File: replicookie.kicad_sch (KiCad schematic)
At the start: 0 parts

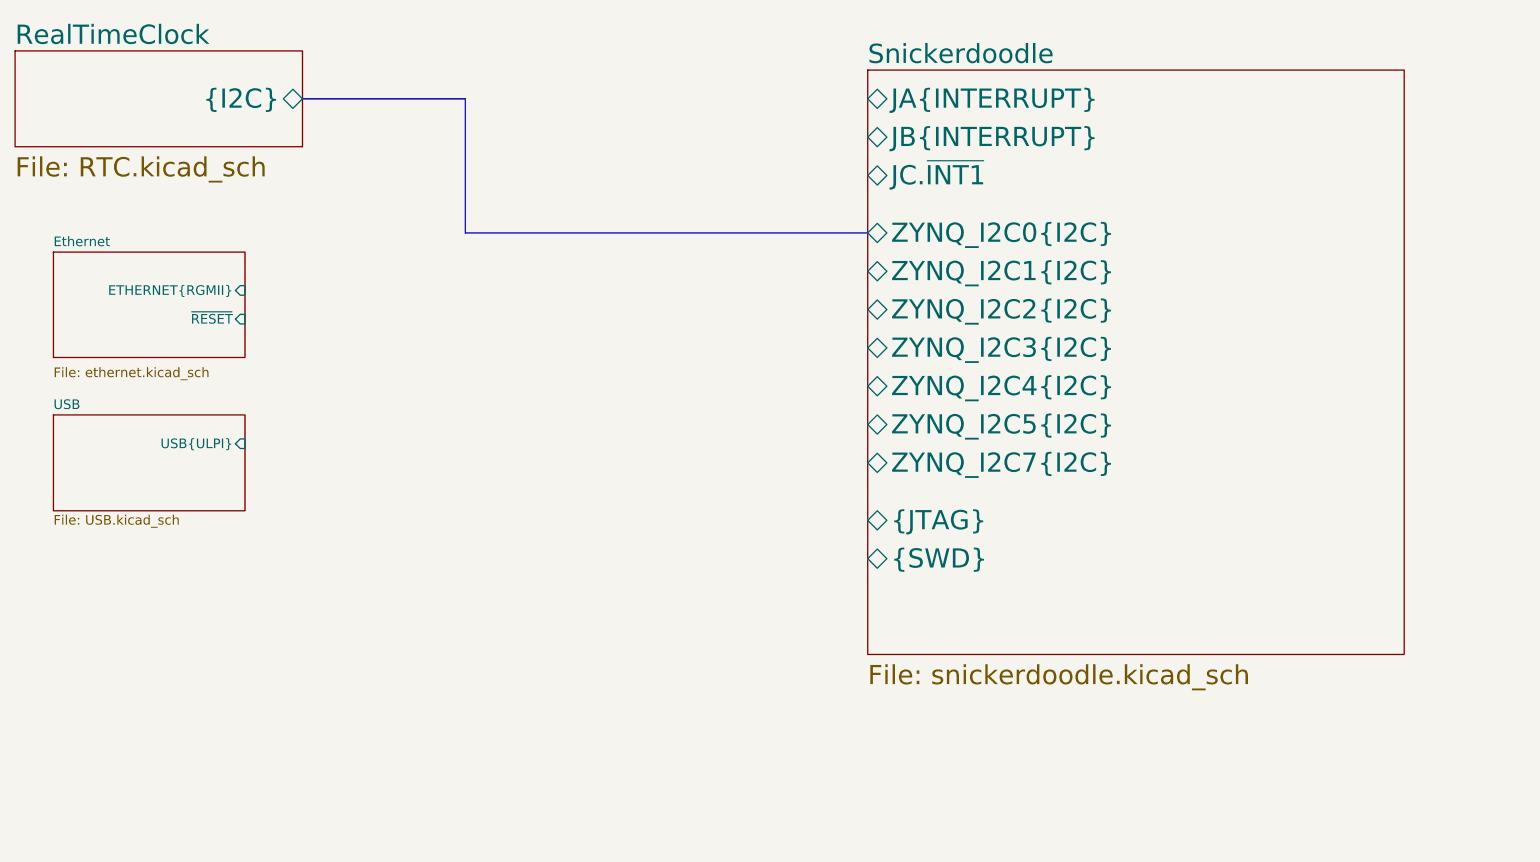
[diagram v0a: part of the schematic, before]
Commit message: Connect Ethernet and USB to MIO, start layout
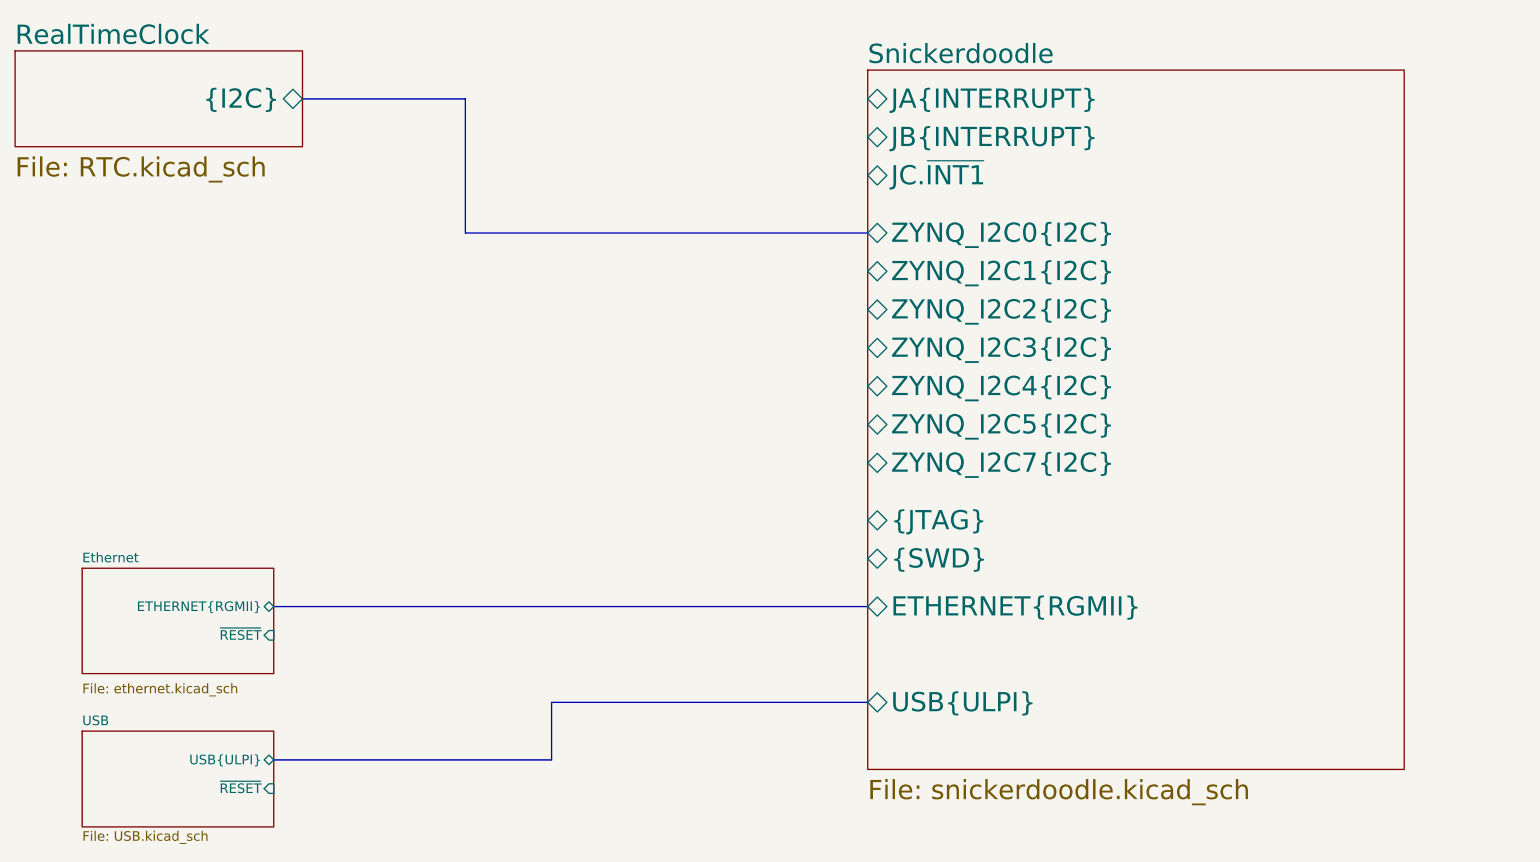
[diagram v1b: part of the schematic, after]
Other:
- sheet Snickerdoodle ports: added ETHERNET{RGMII}, USB{ULPI}; removed none
- sheet USB ports: added ~RESET; removed none

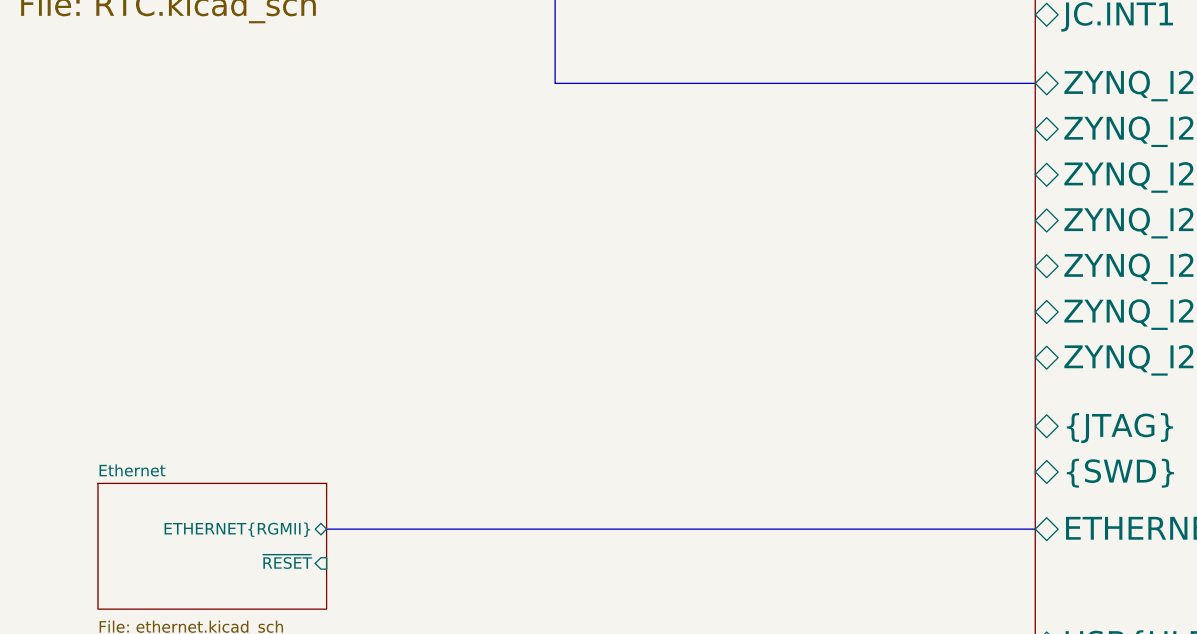
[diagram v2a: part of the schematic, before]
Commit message: Add FTDI chip
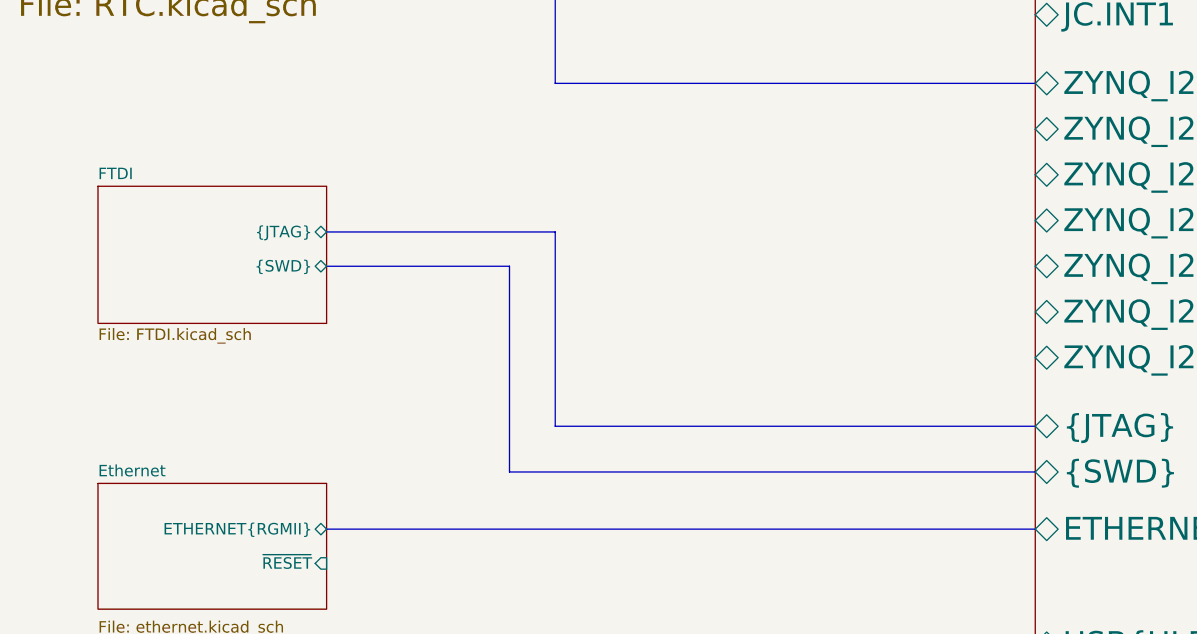
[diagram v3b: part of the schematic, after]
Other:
- added sheet FTDI (FTDI.kicad_sch)

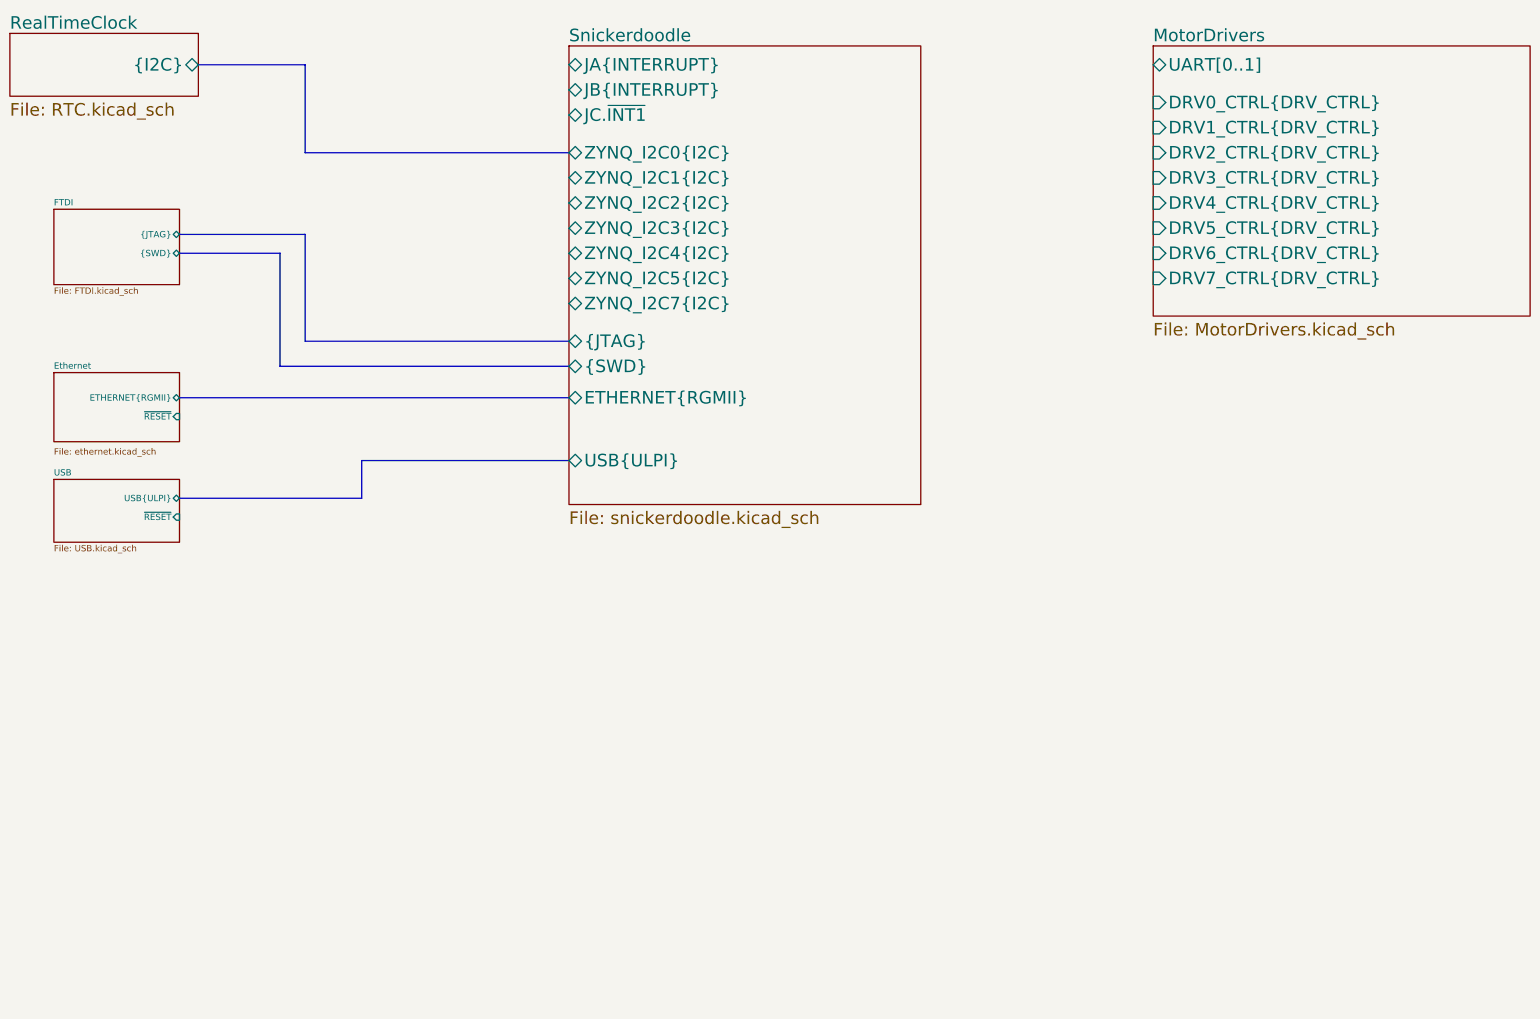
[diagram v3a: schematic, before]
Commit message: Connect Ethernet PHY to FPGA, route RGMII signals
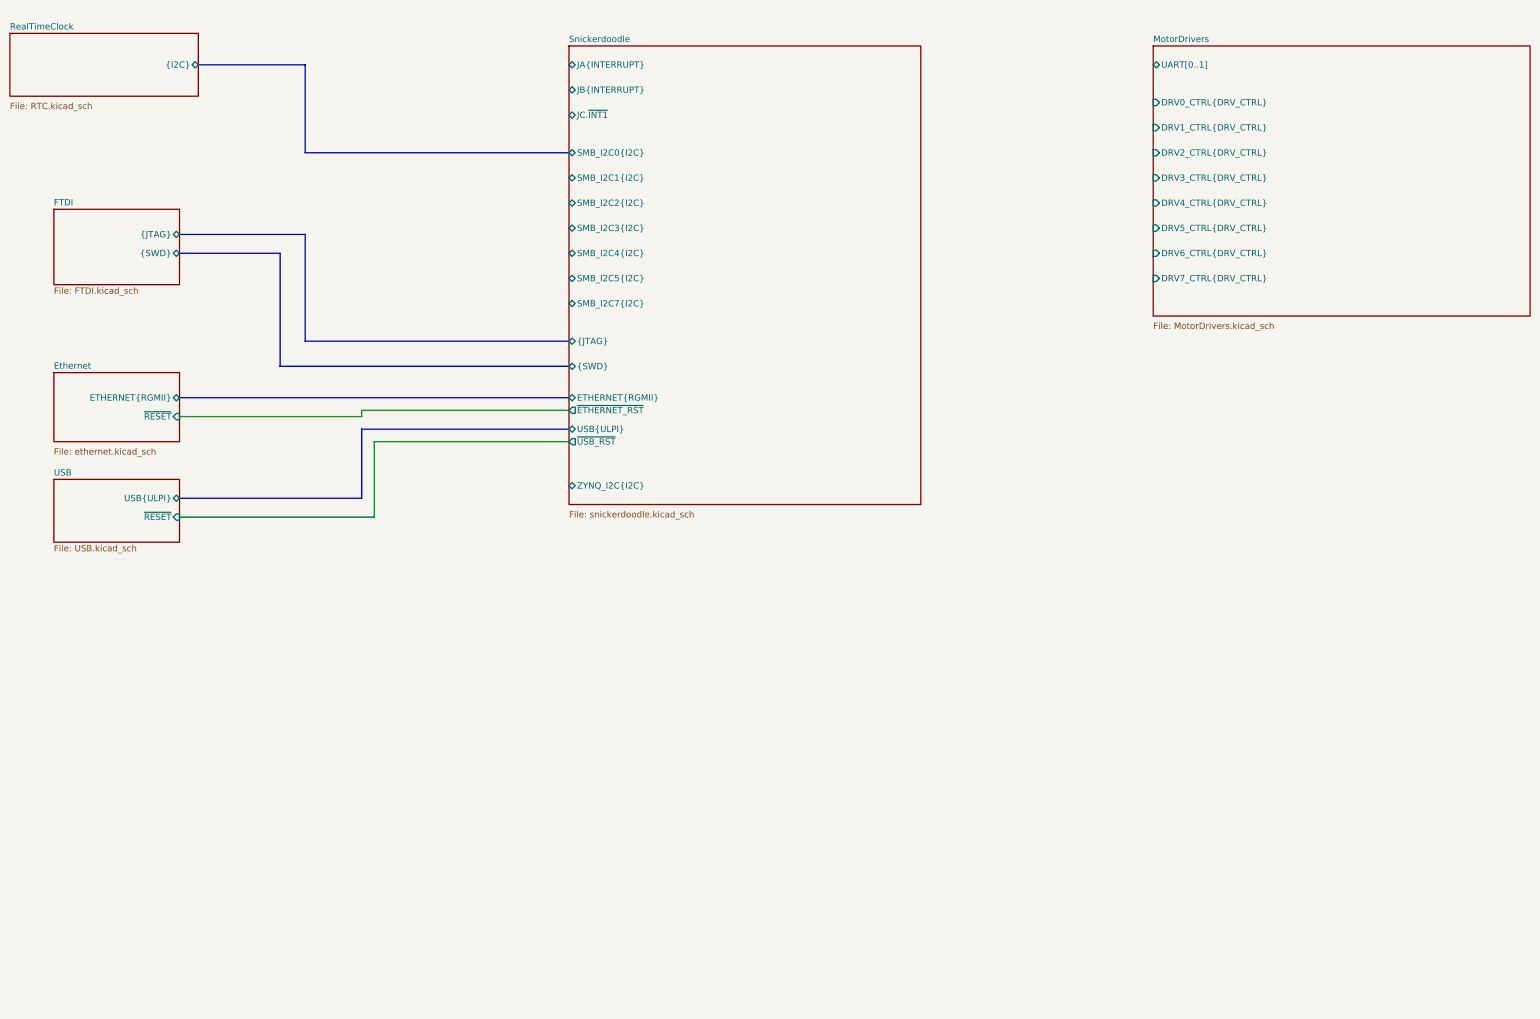
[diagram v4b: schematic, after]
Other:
- sheet Snickerdoodle ports: added SMB_I2C0{I2C}, SMB_I2C1{I2C}, SMB_I2C2{I2C}, SMB_I2C3{I2C}, SMB_I2C4{I2C}, SMB_I2C5{I2C}, SMB_I2C7{I2C}, ZYNQ_I2C{I2C}, ~ETHERNET_RST, ~USB_RST; removed ZYNQ_I2C0{I2C}, ZYNQ_I2C1{I2C}, ZYNQ_I2C2{I2C}, ZYNQ_I2C3{I2C}, ZYNQ_I2C4{I2C}, ZYNQ_I2C5{I2C}, ZYNQ_I2C7{I2C}

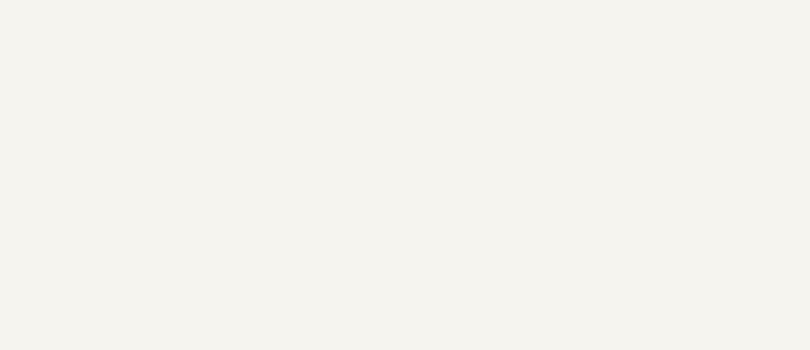
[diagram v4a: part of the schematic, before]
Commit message: Attach ethernet to PL, layout and route
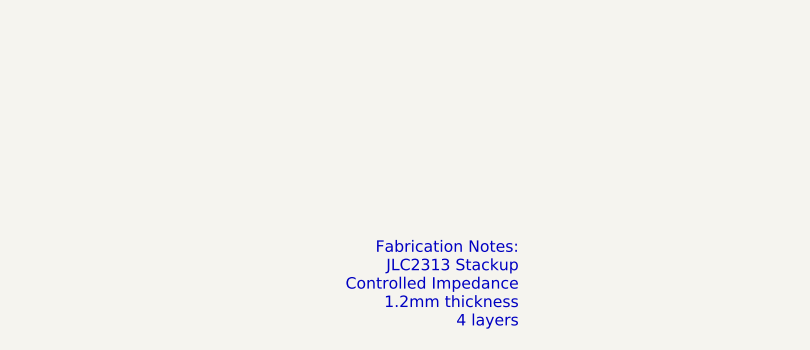
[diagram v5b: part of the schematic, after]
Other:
- note added: "Fabrication Notes: JLC2313 Stackup Controlled Impedance 1.2mm thickness 4 layers"
